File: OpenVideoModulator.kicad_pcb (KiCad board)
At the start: 2 copper layers, 35.3 x 24.9 mm, 25 parts, among them J1 CONN_6, J2 VIDEOCOMP_OUT, J3 SVIDEO_OUT, U1 AD724, Y1 4.433619M

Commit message: Done
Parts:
- J2: value VIDEOCOMP_OUT -> COMPVIDEO_OUT; footprint OpenVideoModulator:SWITCHCRAFT_PJRAN1X1U01X -> OpenVideoModulator:Pin_Header_Straight_1x02-ModSilkS
- J3: footprint OpenVideoModulator:Pin_Header_Straight_1x03-ModSilkS -> OpenVideoModulator:MiniDIN4
- moved J3 9.23 mm to (152.0, 62.0)
- moved J2 8.88 mm to (139.2, 52.5)
- moved C10 7.91 mm to (127.2, 71.8)
- moved C9 7.91 mm to (135.1, 71.8)
- moved V0 4.24 mm to (142.3, 62.0)
- moved R5 3.43 mm to (135.5, 64.0)
- moved R6 3.43 mm to (135.5, 60.6)
- moved H1 3.05 mm to (151.1, 71.4)
- moved H2 3.05 mm to (149.4, 52.8)
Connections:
- J2 pad 1: GND -> Net-(J2-Pad1)
- J2 pad 2: Net-(J2-Pad2) -> GND
- J3 pad 2: Net-(J3-Pad2) -> GND
- R4 pad 1: Net-(J2-Pad2) -> Net-(J2-Pad1)
- R6 pad 1: Net-(J3-Pad2) -> Net-(J3-Pad4)
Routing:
- net Net-(J3-Pad2): track 11.0 -> 0.00 mm
- net Net-(C9-Pad2): track 14.9 -> 5.55 mm
- net Net-(C10-Pad2): track 5.55 -> 14.9 mm
- net Net-(J2-Pad2): track 8.09 -> 0.00 mm
- net Net-(J2-Pad1): track 0.00 -> 6.53 mm
- net Net-(J3-Pad4): track 0.00 -> 5.56 mm
- net /chroma: track 18.9 -> 24.2 mm
- net Net-(J3-Pad3): track 9.11 -> 5.03 mm
- net /luma: track 27.5 -> 25.0 mm
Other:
- board size 35.3 x 24.9 mm -> 38.1 x 24.9 mm
- board text added: "COMP"
- board text removed: "CHROMA"
- board text removed: "LUMA"

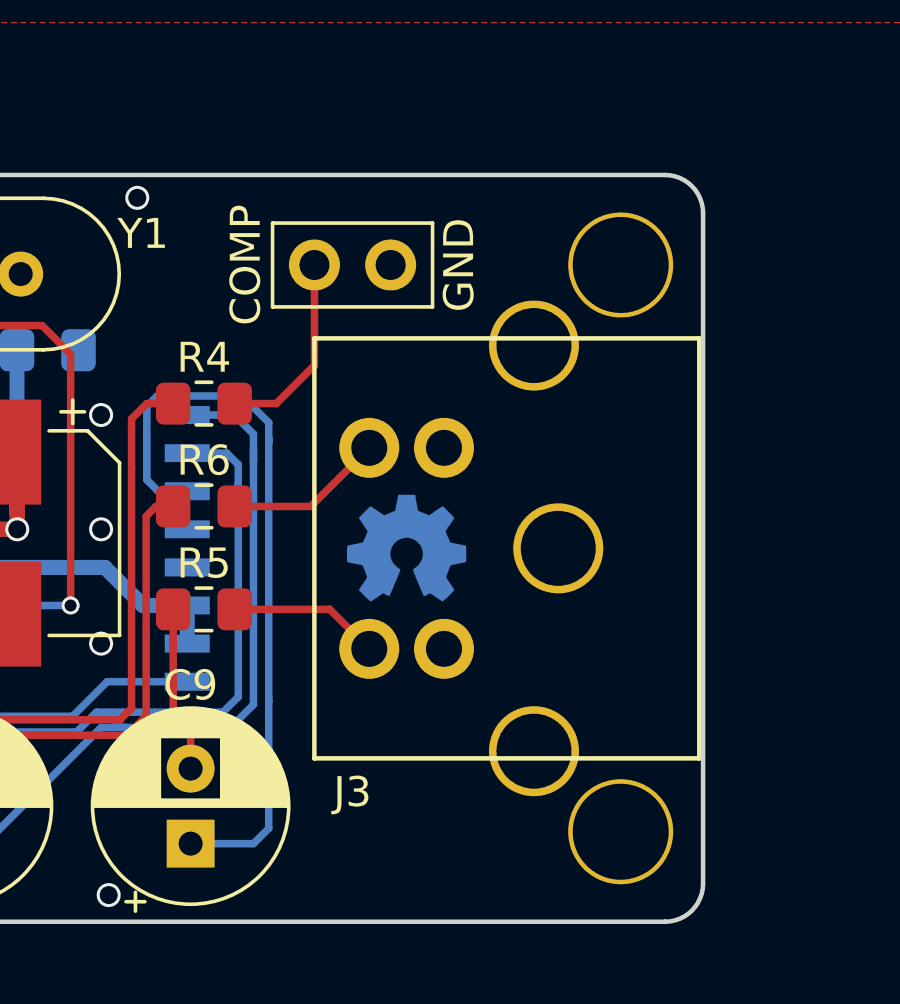
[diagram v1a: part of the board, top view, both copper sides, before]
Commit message: Connect MiniDIN shield
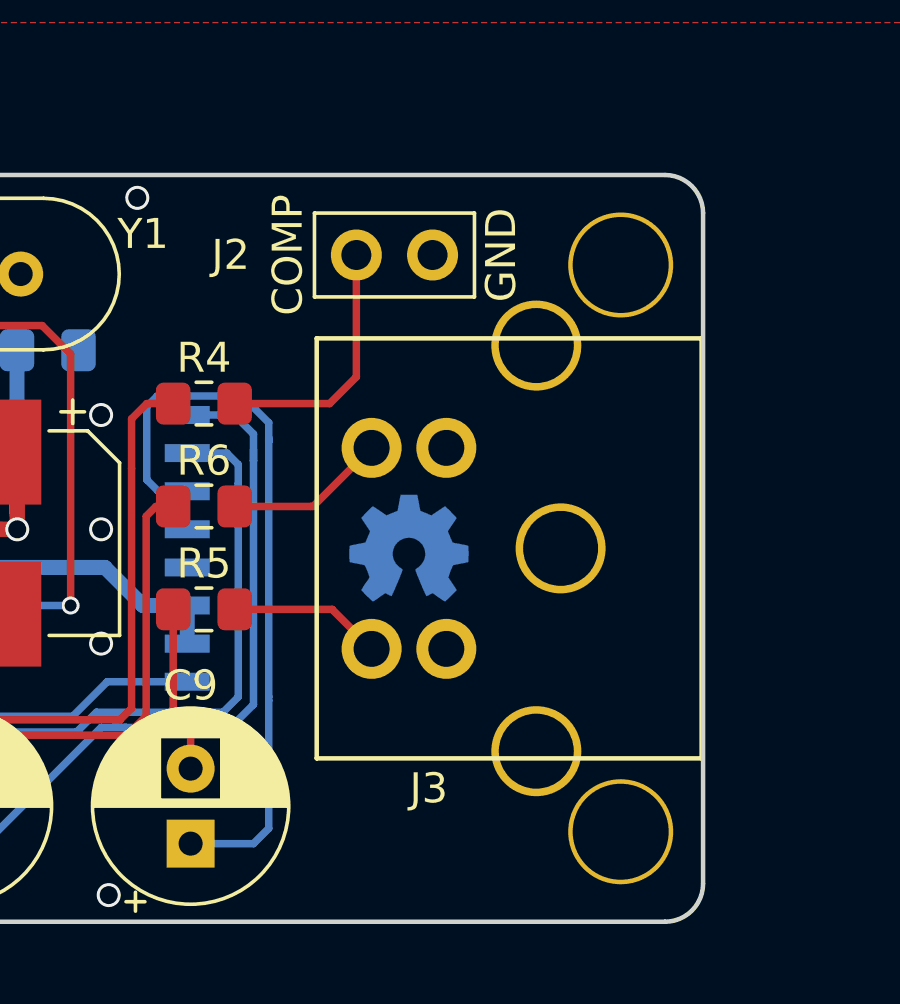
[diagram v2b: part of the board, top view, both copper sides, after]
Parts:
- moved J2 1.44 mm to (140.6, 52.2)
- moved J3 0.08 mm to (152.1, 62.0)
- moved V0 0.08 mm to (142.3, 62.0)
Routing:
- net Net-(J2-Pad1): track 6.53 -> 8.15 mm
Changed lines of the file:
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@@
     (thickness 1.6)
     (drawings 23)
-    (tracks 161)
+    (tracks 162)
     (zones 0)
     (modules 25)
@@
   (title_block
     (title OpenVideoModulator)
-    (date 2019-03-21)
-    (rev 1)
+    (date 2020-03-30)
+    (rev 2)
     (company SukkoPera)
     (comment 1 "Thanks to CPCWiki")
@@
   )
   (module OpenVideoModulator:oshw_logo (layer B.Cu)
-    (at 142.269551 61.976 180)
+    (at 142.347551 61.976 180)
     (descr "Open  Source  Hardware  Symbol")
     (tags "Logo  Symbol  OSHW")
@@
   )
   (module OpenVideoModulator:Pin_Header_Straight_1x02-ModSilkS (layer F.Cu)
-    (at 139.192 52.53 90)
+    (at 140.589 52.196999 90)
     (descr "Through hole straight pin header, 1x02, 2.54mm pitch, single row")
     (tags "Through hole pin header THT 1x02 2.54mm single row")
-    (fp_text reference J2 (at 2.286 1.27) (layer F.SilkS) hide
+    (fp_text reference J2 (at -0.000001 -4.191) (layer F.SilkS)
       (effects (font (size 1 1) (thickness 0.15)))
     )
@@
   )
   (module OpenVideoModulator:MiniDIN4 (layer F.Cu)
-    (at 152.019 61.976 270)
+    (at 152.097 61.976 270)
     (descr "TE Connectivity 5749181-1")
     (tags "DIN MiniDIN SVideo S-Video")
-    (fp_text reference J3 (at 8.128 11.557 180) (layer F.SilkS)
+    (fp_text reference J3 (at 8.001 9.095 180) (layer F.SilkS)
       (effects (font (size 1 1) (thickness 0.15)))
     )
@@
     (fp_line (start 7 12.83) (end 7 0) (layer F.CrtYd) (width 0.12))
     (fp_line (start 7 0) (end -7 0) (layer F.CrtYd) (width 0.12))
-    (pad 5 thru_hole circle (at -6.76 5.51 270) (size 3 3) (drill 2.5) (layers *.Cu *.Mask))
-    (pad 5 thru_hole circle (at 0 4.7 270) (size 3 3) (drill 2.5) (layers *.Cu *.Mask))
-    (pad 5 thru_hole circle (at 6.76 5.51 270) (size 3 3) (drill 2.5) (layers *.Cu *.Mask))
+    (pad 0 thru_hole circle (at -6.76 5.51 270) (size 3 3) (drill 2.5) (layers *.Cu *.Mask)
+      (net 2 GND))
+    (pad 0 thru_hole circle (at 0 4.7 270) (size 3 3) (drill 2.5) (layers *.Cu *.Mask)
+      (net 2 GND))
+    (pad 0 thru_hole circle (at 6.76 5.51 270) (size 3 3) (drill 2.5) (layers *.Cu *.Mask)
+      (net 2 GND))
     (pad 2 thru_hole circle (at -3.35 8.51 270) (size 2 2) (drill 1.2) (layers *.Cu *.Mask)
       (net 2 GND))
@@
     )
   )
-  (gr_text GND (at 144.018 52.530001 90) (layer F.SilkS)
+  (gr_text GND (at 145.415 52.197 90) (layer F.SilkS)
     (effects (font (size 1 1) (thickness 0.15)))
   )
-  (gr_text COMP (at 136.906 52.53 90) (layer F.SilkS)
+  (gr_text COMP (at 138.303 52.196999 90) (layer F.SilkS)
     (effects (font (size 1 1) (thickness 0.15)))
   )
@@
   (segment (start 119.507 66.421) (end 124.079 66.421) (width 0.25) (layer F.Cu) (net 14))
   (segment (start 124.079 66.421) (end 125.652 66.421) (width 0.25) (layer B.Cu) (net 14) (status 20))
-  (segment (start 139.701 64.008) (end 141.019 65.326) (width 0.25) (layer F.Cu) (net 15))
-  (segment (start 136.534 64.008) (end 139.701 64.008) (width 0.25) (layer F.Cu) (net 15))
+  (segment (start 139.779 64.008) (end 141.097 65.326) (width 0.25) (layer F.Cu) (net 15))
+  (segment (start 136.534 64.008) (end 139.779 64.008) (width 0.25) (layer F.Cu) (net 15))
   (segment (start 136.534 60.579) (end 136.534 60.715) (width 0.25) (layer F.Cu) (net 20) (status 30))
   (segment (start 136.534 60.715) (end 136.661 60.715) (width 0.25) (layer F.Cu) (net 20) (status 30))
@@
   (segment (start 137.668 58.42) (end 137.668 66.929) (width 0.25) (layer B.Cu) (net 17))
   (segment (start 133.985 60.071) (end 133.604 59.69) (width 0.25) (layer B.Cu) (net 17))
-  (segment (start 134.952 60.071) (end 133.985 60.071) (width 0.25) (layer B.Cu) (net 17))
+  (segment (start 134.952 60.071) (end 133.985 60.071) (width 0.25) (layer B.Cu) (net 17) (status 10))
   (segment (start 137.668 57.785) (end 137.668 58.42) (width 0.25) (layer B.Cu) (net 17))
   (segment (start 137.668 58.293) (end 137.668 58.42) (width 0.25) (layer B.Cu) (net 17))
   (segment (start 133.604 59.69) (end 133.604 57.243998) (width 0.25) (layer B.Cu) (net 17))
-  (segment (start 134.952 57.531) (end 136.525 57.531) (width 0.25) (layer B.Cu) (net 18))
+  (segment (start 134.952 57.531) (end 136.525 57.531) (width 0.25) (layer B.Cu) (net 18) (status 10))
   (segment (start 136.525 57.531) (end 137.16 58.166) (width 0.25) (layer B.Cu) (net 18))
   (segment (start 137.16 58.166) (end 137.16 59.055) (width 0.25) (layer B.Cu) (net 18))
   (segment (start 137.16 67.183) (end 137.16 59.055) (width 0.25) (layer B.Cu) (net 18))
   (segment (start 137.16 59.055) (end 137.16 58.674) (width 0.25) (layer B.Cu) (net 18))
-  (segment (start 136.534 57.15) (end 137.922 57.15) (width 0.25) (layer F.Cu) (net 19))
-  (segment (start 139.192 55.88) (end 139.192 52.53) (width 0.25) (layer F.Cu) (net 19))
-  (segment (start 137.922 57.15) (end 139.192 55.88) (width 0.25) (layer F.Cu) (net 19))
-  (segment (start 139.066 60.579) (end 141.019 58.626) (width 0.25) (layer F.Cu) (net 20))
-  (segment (start 136.534 60.579) (end 139.066 60.579) (width 0.25) (layer F.Cu) (net 20))
+  (segment (start 136.534 57.15) (end 139.7 57.15) (width 0.25) (layer F.Cu) (net 19) (status 10))
+  (segment (start 140.589 56.261) (end 140.589 52.53) (width 0.25) (layer F.Cu) (net 19) (status 20))
+  (segment (start 139.7 57.15) (end 140.589 56.261) (width 0.25) (layer F.Cu) (net 19))
+  (segment (start 136.534 60.579) (end 139.066 60.579) (width 0.25) (layer F.Cu) (net 20) (status 10))
+  (segment (start 139.144 60.579) (end 141.097 58.626) (width 0.25) (layer F.Cu) (net 20))
+  (segment (start 139.066 60.579) (end 139.144 60.579) (width 0.25) (layer F.Cu) (net 20))
   (zone (net 2) (net_name GND) (layer B.Cu) (hatch edge 0.508)
     (connect_pads (clearance 0.1))
